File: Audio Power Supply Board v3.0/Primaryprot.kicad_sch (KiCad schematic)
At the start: 4 parts, among them Q13 MPSA06

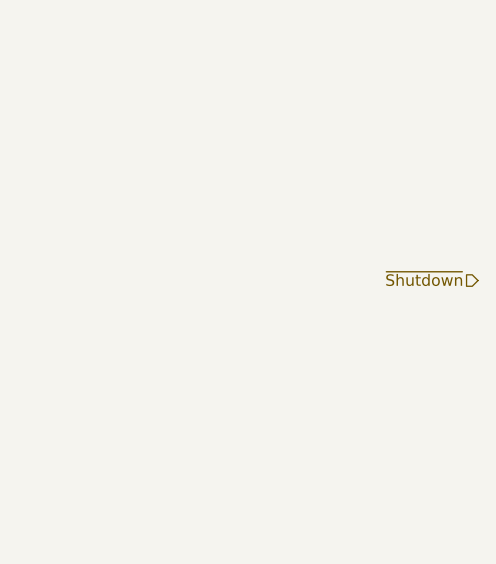
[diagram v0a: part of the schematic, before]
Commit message: Add protection circuits
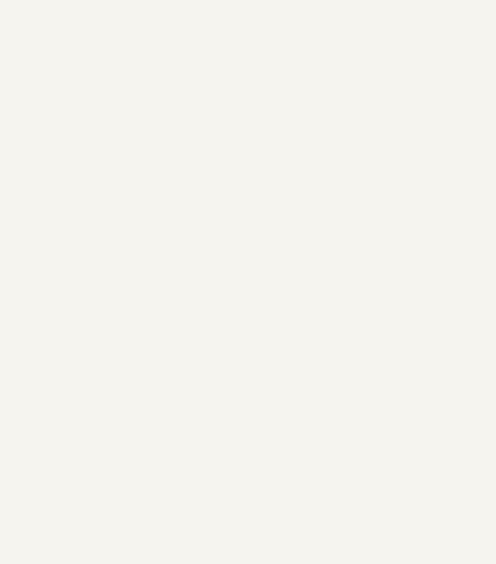
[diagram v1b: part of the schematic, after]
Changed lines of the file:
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@@
-    (effects (font (size 1.27 1.27)) (justify right))
-  )
-  (hierarchical_label "~Shutdown" (shape input) (at 245.745 64.77 180)
     (effects (font (size 1.27 1.27)) (justify right))
   )
